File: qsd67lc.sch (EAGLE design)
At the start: 65 parts, among them CON1 RIA-AKL-230-04, CON2 RIA-AKL-230-04, CON3 RIA-AKL-230-03, IC1 MEGA8-P, IC2 BTS555E3146, IC3 MAX3232CPE, IC4 LM2576S, IC5 FT232RL, IC6 ISO7221A, T1 BCR141, U1 HC_05, X2 RS232

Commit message: first placement of all parts
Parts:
- LED4: value (none) -> green
- LED5: value (none) -> orange
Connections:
- net N$25 renamed USB_TX_LED
- net RS232_RX: no longer IC6.OUTA
- net RS232_TX: no longer IC6.INB
- net RXD_RS232: now also IC6.OUTA
- net TXD_RS232: now also IC6.INB
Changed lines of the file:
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@@
 <part name="C13" library="rcl" library_urn="urn:adsk.eagle:library:334" deviceset="C-EU" device="C0805" package3d_urn="urn:adsk.eagle:package:23617/2" value="100nF"/>
 <part name="C14" library="rcl" library_urn="urn:adsk.eagle:library:334" deviceset="C-EU" device="C0805" package3d_urn="urn:adsk.eagle:package:23617/2" value="100nF"/>
-<part name="LED4" library="led" library_urn="urn:adsk.eagle:library:259" deviceset="LED" device="SML0805" package3d_urn="urn:adsk.eagle:package:15830/1"/>
-<part name="LED5" library="led" library_urn="urn:adsk.eagle:library:259" deviceset="LED" device="SML0805" package3d_urn="urn:adsk.eagle:package:15830/1"/>
+<part name="LED4" library="led" library_urn="urn:adsk.eagle:library:259" deviceset="LED" device="SML0805" package3d_urn="urn:adsk.eagle:package:15830/1" value="green"/>
+<part name="LED5" library="led" library_urn="urn:adsk.eagle:library:259" deviceset="LED" device="SML0805" package3d_urn="urn:adsk.eagle:package:15830/1" value="orange"/>
 <part name="R18" library="rcl" library_urn="urn:adsk.eagle:library:334" deviceset="R-EU_" device="R0805" package3d_urn="urn:adsk.eagle:package:23553/2" value="270R"/>
 <part name="R19" library="rcl" library_urn="urn:adsk.eagle:library:334" deviceset="R-EU_" device="R0805" package3d_urn="urn:adsk.eagle:package:23553/2" value="270R"/>
@@
 <pinref part="R18" gate="G$1" pin="1"/>
 <wire x1="60.96" y1="10.16" x2="60.96" y2="0" width="0.1524" layer="91"/>
-</segment>
-</net>
-<net name="N$25" class="0">
+<label x="22.86" y="0" size="1.778" layer="95"/>
+</segment>
+</net>
+<net name="USB_TX_LED" class="0">
 <segment>
 <pinref part="IC5" gate="1" pin="CBUS1"/>
@@
 <pinref part="R19" gate="G$1" pin="1"/>
 <wire x1="68.58" y1="10.16" x2="68.58" y2="-2.54" width="0.1524" layer="91"/>
+<label x="22.86" y="-2.54" size="1.778" layer="95"/>
 </segment>
 </net>
@@
 </segment>
 </net>
-<net name="RS232_RX" class="0">
+<net name="RXD_RS232" class="0">
 <segment>
 <pinref part="IC6" gate="G$1" pin="OUTA"/>
@@
 </segment>
 </net>
-<net name="RS232_TX" class="0">
+<net name="TXD_RS232" class="0">
 <segment>
 <pinref part="IC6" gate="G$1" pin="INB"/>

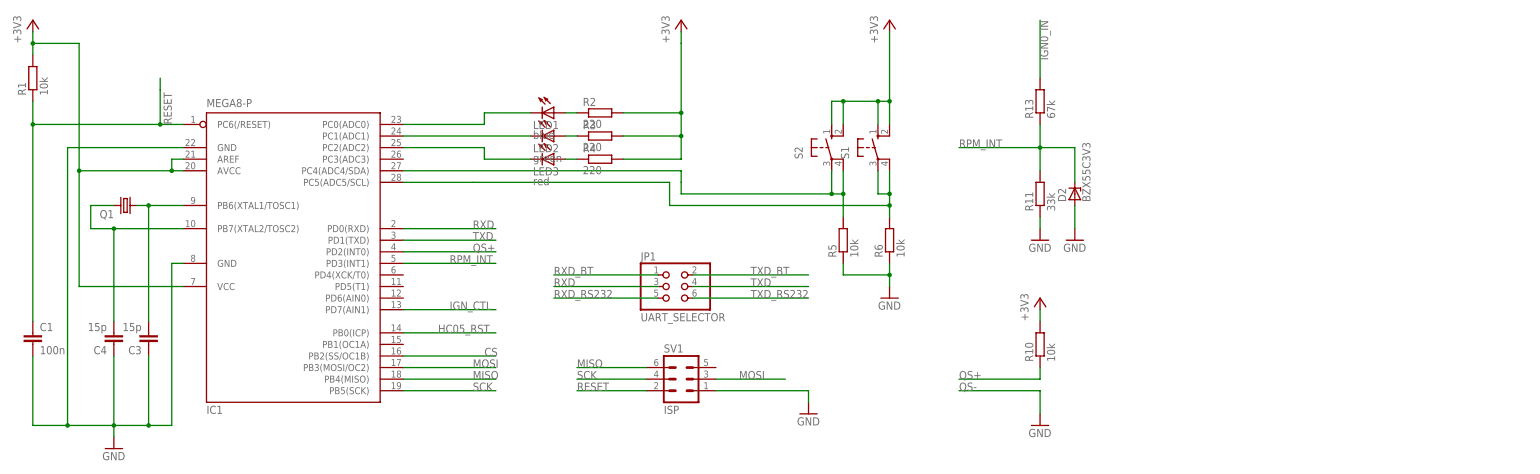
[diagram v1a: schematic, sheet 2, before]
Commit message: working commit: * moved drill hole * removed 1 button * replaced status leds * moved ground planes
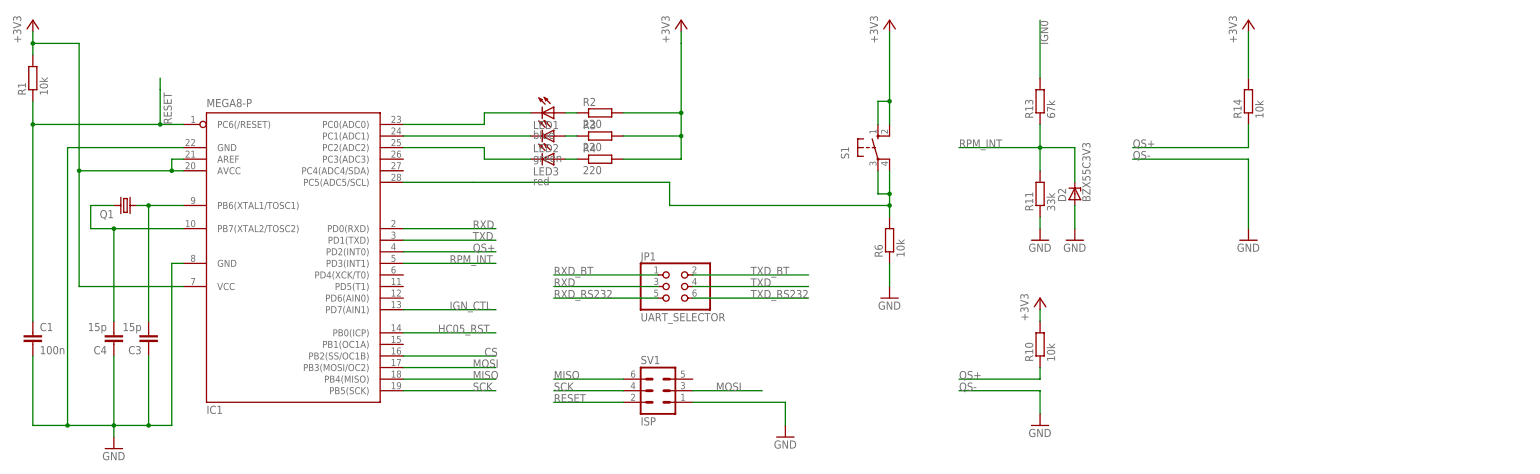
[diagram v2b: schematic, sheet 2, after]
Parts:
- removed H2: MOUNT-HOLE3.0, holes:MOUNT-HOLE3.0
- removed R5: 10k, rcl:R-EU_R0805
- removed S2: (no value), switch-omron:10-XX
- added R14: 10k, rcl:R-EU_R0805
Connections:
- removed net IGN0_IN: R13.2
- removed net N$8: IC1.PC4(ADC4/SDA), R5.2, S2.P, S2.P1
- net +3V3: now also R14.2; no longer S2.S, S2.S1
- net GND: no longer R5.1
- net IGN0: now also R13.2
- net QS+: now also R14.1
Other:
- moved on the sheet: SV1

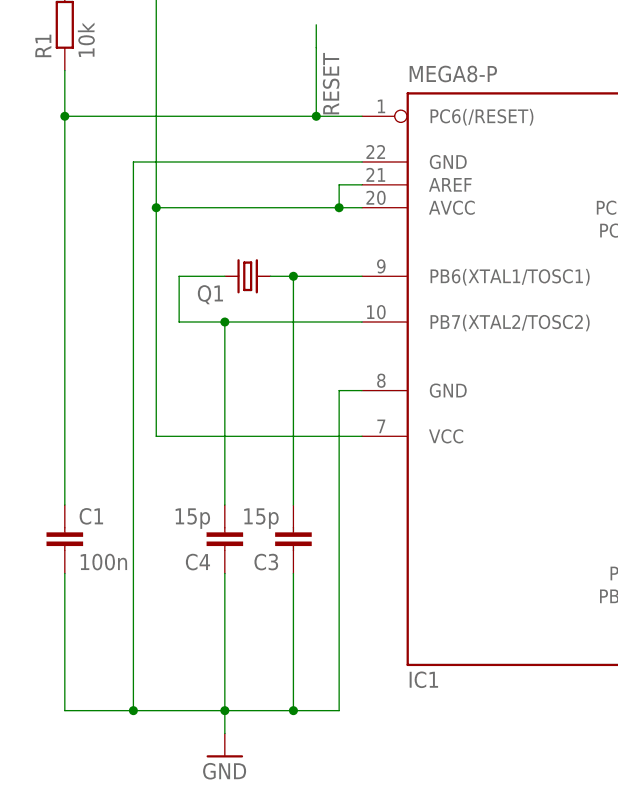
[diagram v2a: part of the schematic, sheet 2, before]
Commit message: routed ftdi part
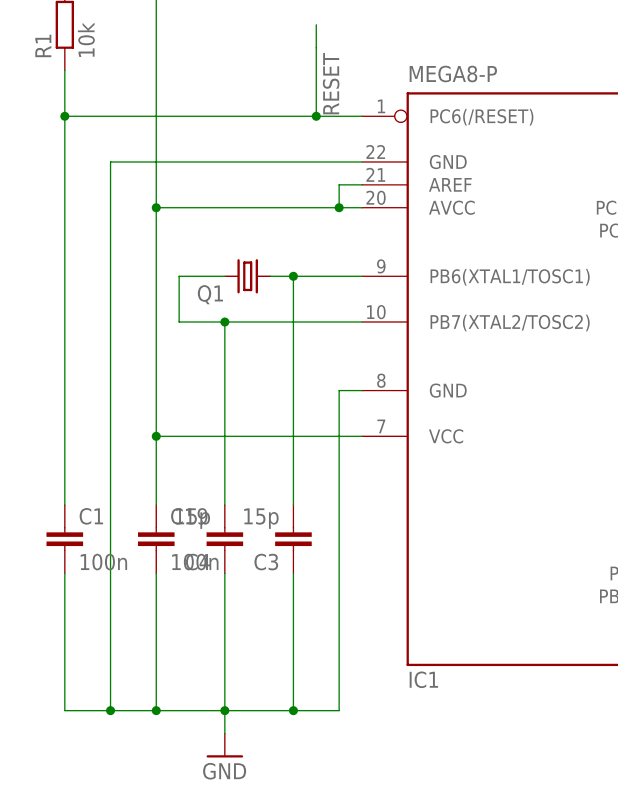
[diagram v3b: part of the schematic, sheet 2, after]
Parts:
- added C19: 100n, rcl:C-EUC0805
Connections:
- net +3V3: now also C19.1
- net GND: now also C19.2
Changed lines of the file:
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@@
 <part name="+3V9" library="supply1" library_urn="urn:adsk.eagle:library:371" deviceset="+3V3" device=""/>
 <part name="GND22" library="supply1" library_urn="urn:adsk.eagle:library:371" deviceset="GND" device=""/>
+<part name="C19" library="rcl" library_urn="urn:adsk.eagle:library:334" deviceset="C-EU" device="C0805" package3d_urn="urn:adsk.eagle:package:23617/2" value="100n"/>
 </parts>
 <sheets>
@@
 <instance part="GND22" gate="1" x="208.28" y="5.08">
 <attribute name="VALUE" x="205.74" y="2.54" size="1.778" layer="96"/>
+</instance>
+<instance part="C19" gate="G$1" x="-48.26" y="-15.24">
+<attribute name="NAME" x="-46.736" y="-14.859" size="1.778" layer="95"/>
+<attribute name="VALUE" x="-46.736" y="-19.939" size="1.778" layer="96"/>
 </instance>
 </instances>
@@
 <pinref part="C1" gate="G$1" pin="2"/>
 <wire x1="-58.42" y1="-20.32" x2="-58.42" y2="-35.56" width="0.1524" layer="91"/>
-<wire x1="-58.42" y1="-35.56" x2="-50.8" y2="-35.56" width="0.1524" layer="91"/>
+<wire x1="-58.42" y1="-35.56" x2="-53.34" y2="-35.56" width="0.1524" layer="91"/>
 <pinref part="IC1" gate="G$1" pin="GND"/>
-<wire x1="-50.8" y1="-35.56" x2="-40.64" y2="-35.56" width="0.1524" layer="91"/>
-<wire x1="-25.4" y1="25.4" x2="-50.8" y2="25.4" width="0.1524" layer="91"/>
-<wire x1="-50.8" y1="25.4" x2="-50.8" y2="-35.56" width="0.1524" layer="91"/>
-<junction x="-50.8" y="-35.56"/>
+<wire x1="-53.34" y1="-35.56" x2="-48.26" y2="-35.56" width="0.1524" layer="91"/>
+<wire x1="-48.26" y1="-35.56" x2="-40.64" y2="-35.56" width="0.1524" layer="91"/>
+<wire x1="-25.4" y1="25.4" x2="-53.34" y2="25.4" width="0.1524" layer="91"/>
+<wire x1="-53.34" y1="25.4" x2="-53.34" y2="-35.56" width="0.1524" layer="91"/>
+<junction x="-53.34" y="-35.56"/>
+<pinref part="C19" gate="G$1" pin="2"/>
+<wire x1="-48.26" y1="-20.32" x2="-48.26" y2="-35.56" width="0.1524" layer="91"/>
+<junction x="-48.26" y="-35.56"/>
 </segment>
 <segment>
@@
 <junction x="-48.26" y="20.32"/>
 <pinref part="+3V2" gate="G$1" pin="+3V3"/>
-</segment>
-<segment>
+<pinref part="C19" gate="G$1" pin="1"/>
+<wire x1="-48.26" y1="-5.08" x2="-48.26" y2="-12.7" width="0.1524" layer="91"/>
+<junction x="-48.26" y="-5.08"/>
+</segment>
+<segment>

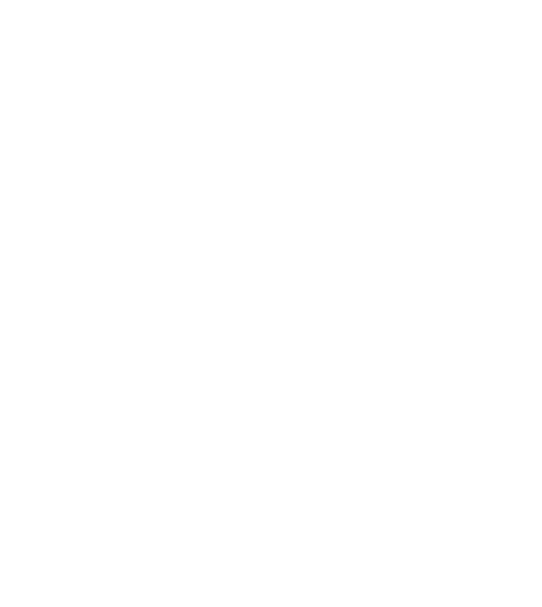
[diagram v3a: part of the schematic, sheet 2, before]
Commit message: finished layout added some test probe pins to 3v3 12V and GND added lables to leds, connectors and pinheads
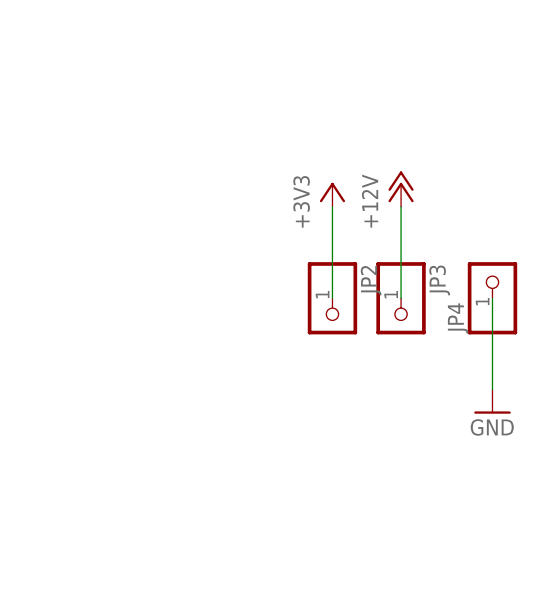
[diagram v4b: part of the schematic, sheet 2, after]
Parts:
- added JP2, JP3, JP4: (no value), pinhead:PINHD-1X1
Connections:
- net +12V: now also JP3.1
- net +3V3: now also JP2.1
- net GND: now also JP4.1
